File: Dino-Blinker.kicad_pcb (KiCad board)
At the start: 2 copper layers, 63.5 x 34.4 mm, 26 parts, among them IC1 M74HC4060YRM13TR, J1 Conn_01x02_Pin

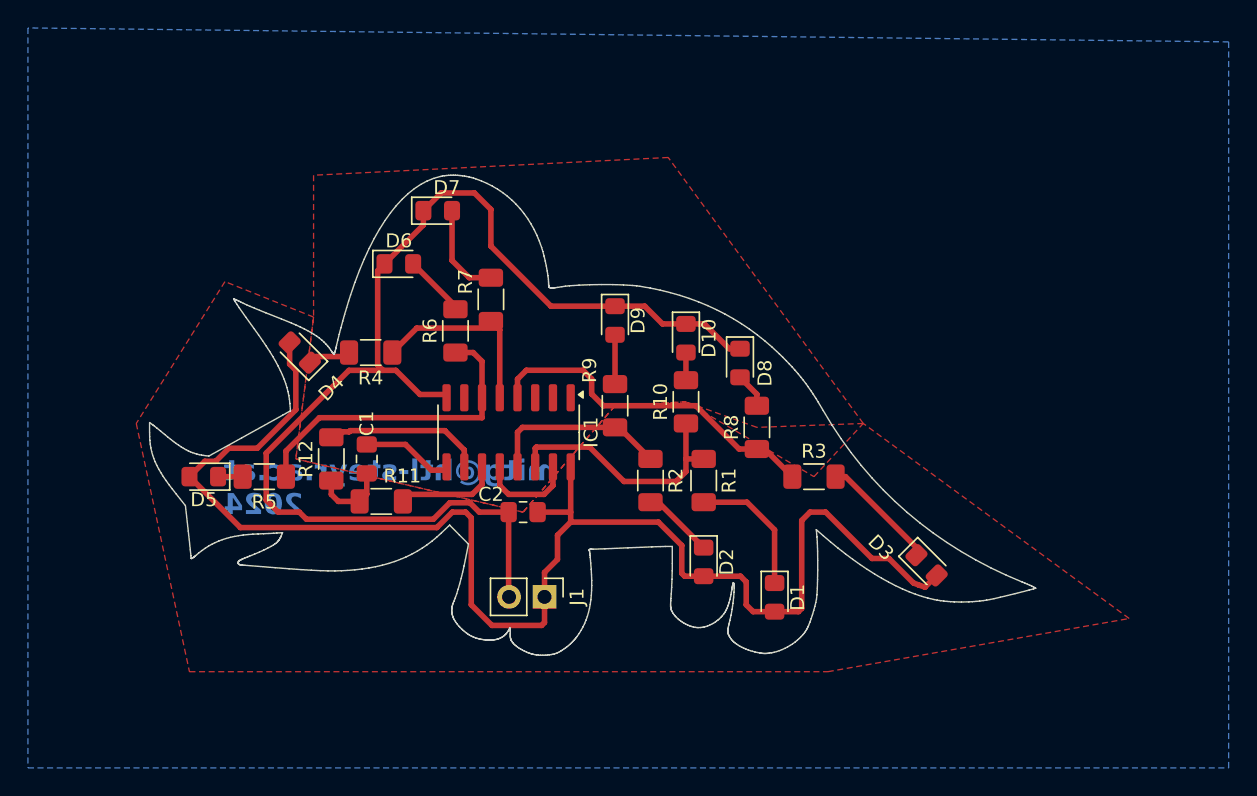
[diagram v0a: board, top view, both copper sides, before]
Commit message: 0402er Leds
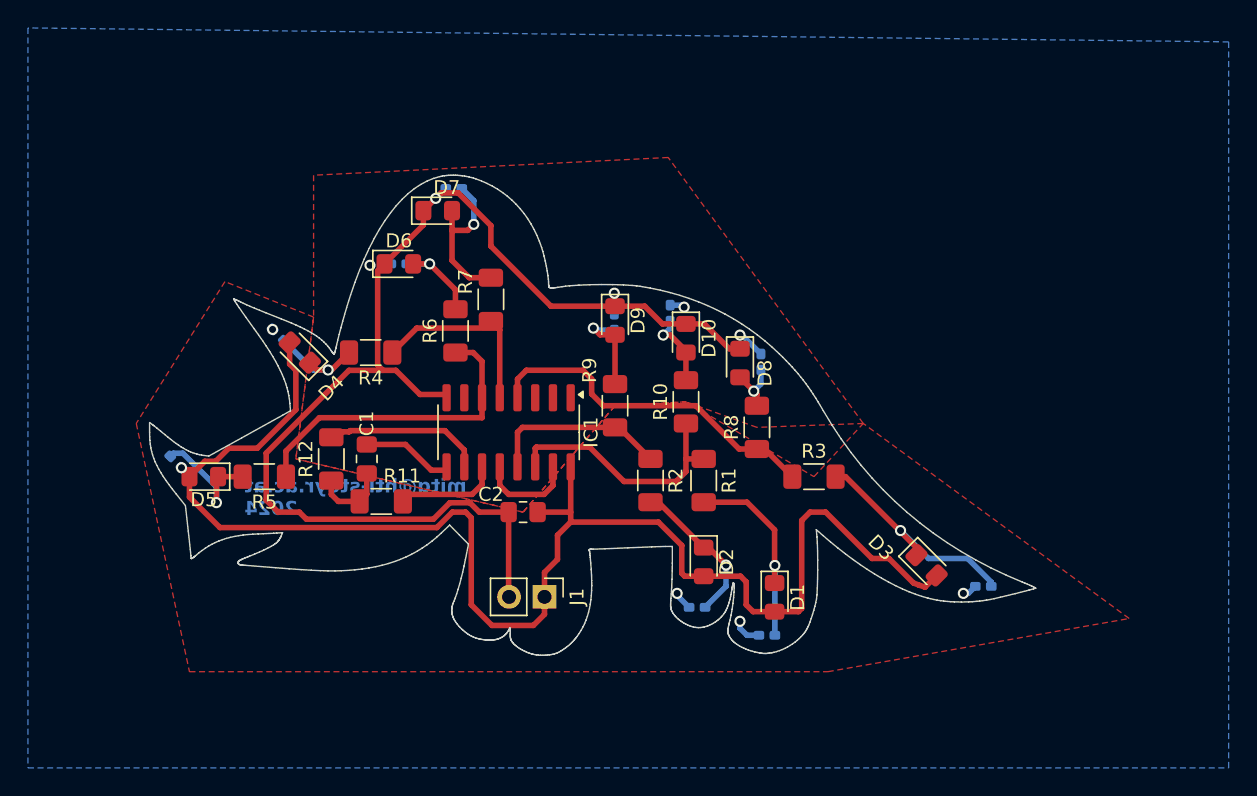
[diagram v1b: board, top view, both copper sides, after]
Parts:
- added D11: LED, LED_SMD:LED_0402_1005Metric_Pad0.77x0.64mm_HandSolder, B.Cu at (156.9, 115.5)
- added D12: LED, LED_SMD:LED_0402_1005Metric_Pad0.77x0.64mm_HandSolder, B.Cu at (151.9, 113.5)
- added D13: LED, LED_SMD:LED_0402_1005Metric_Pad0.77x0.64mm_HandSolder, B.Cu at (172.4, 112.0)
- added D14: LED, LED_SMD:LED_0402_1005Metric_Pad0.77x0.64mm_HandSolder, B.Cu at (121.9, 94.0)
- added D15: LED, LED_SMD:LED_0402_1005Metric_Pad0.77x0.64mm_HandSolder, B.Cu at (114.6, 103.1)
- added D16: LED, LED_SMD:LED_0402_1005Metric_Pad0.77x0.64mm_HandSolder, B.Cu at (130.6, 88.9)
- added D17: LED, LED_SMD:LED_0402_1005Metric_Pad0.77x0.64mm_HandSolder, B.Cu at (134.5, 83.5)
- added D18: LED, LED_SMD:LED_0402_1005Metric_Pad0.77x0.64mm_HandSolder, B.Cu at (156.5, 95.9)
- added D19: LED, LED_SMD:LED_0402_1005Metric_Pad0.77x0.64mm_HandSolder, B.Cu at (146.0, 93.1)
- added D20: LED, LED_SMD:LED_0402_1005Metric_Pad0.77x0.64mm_HandSolder, B.Cu at (150.0, 92.4)
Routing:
- net Net-(D13-K): track 8.44 -> 16.8 mm, vias 0 -> 1
- net Net-(D15-K): track 1.76 -> 9.20 mm, vias 0 -> 1
- net Net-(D12-K): track 5.16 -> 10.9 mm, vias 0 -> 1
- net Net-(D1-K): track 9.71 -> 14.7 mm, vias 0 -> 1
- net VCC: track 103.3 -> 108.3 mm, vias 0 -> 5
- net Net-(D17-A): track 6.86 -> 11.5 mm, vias 0 -> 1
- net Net-(D14-K): track 3.11 -> 7.58 mm, vias 0 -> 1
- net GND: track 86.8 -> 90.8 mm, vias 0 -> 5
- net Net-(D19-A): track 3.53 -> 6.84 mm, vias 0 -> 1
- net Net-(D10-A): track 1.98 -> 5.29 mm, vias 0 -> 1
- net Net-(D16-A): track 4.51 -> 6.83 mm, vias 0 -> 1
- net Net-(D18-A): track 2.54 -> 4.26 mm, vias 0 -> 1
